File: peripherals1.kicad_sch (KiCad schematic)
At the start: 39 parts, among them Q1 Q_NMOS_GSD, SW3 SW_Push, SW4 SW_Push, SW5 SW_Push, SW6 SW_Push, U7 TSDP343xx

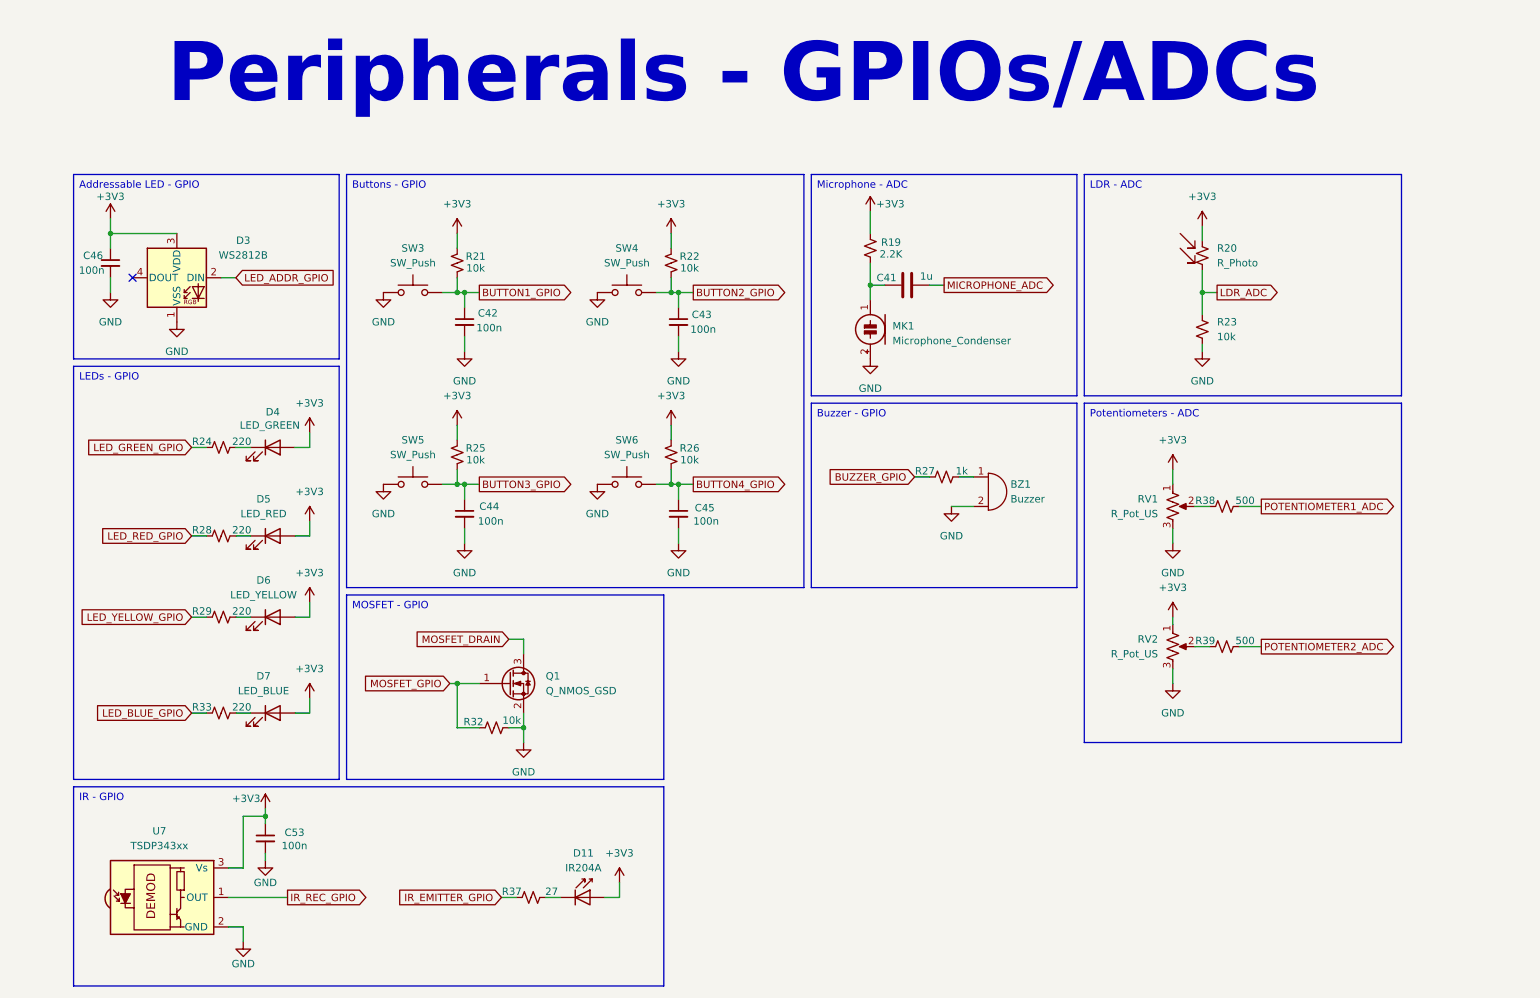
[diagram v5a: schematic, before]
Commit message: feat: adds footprints and new light sensor
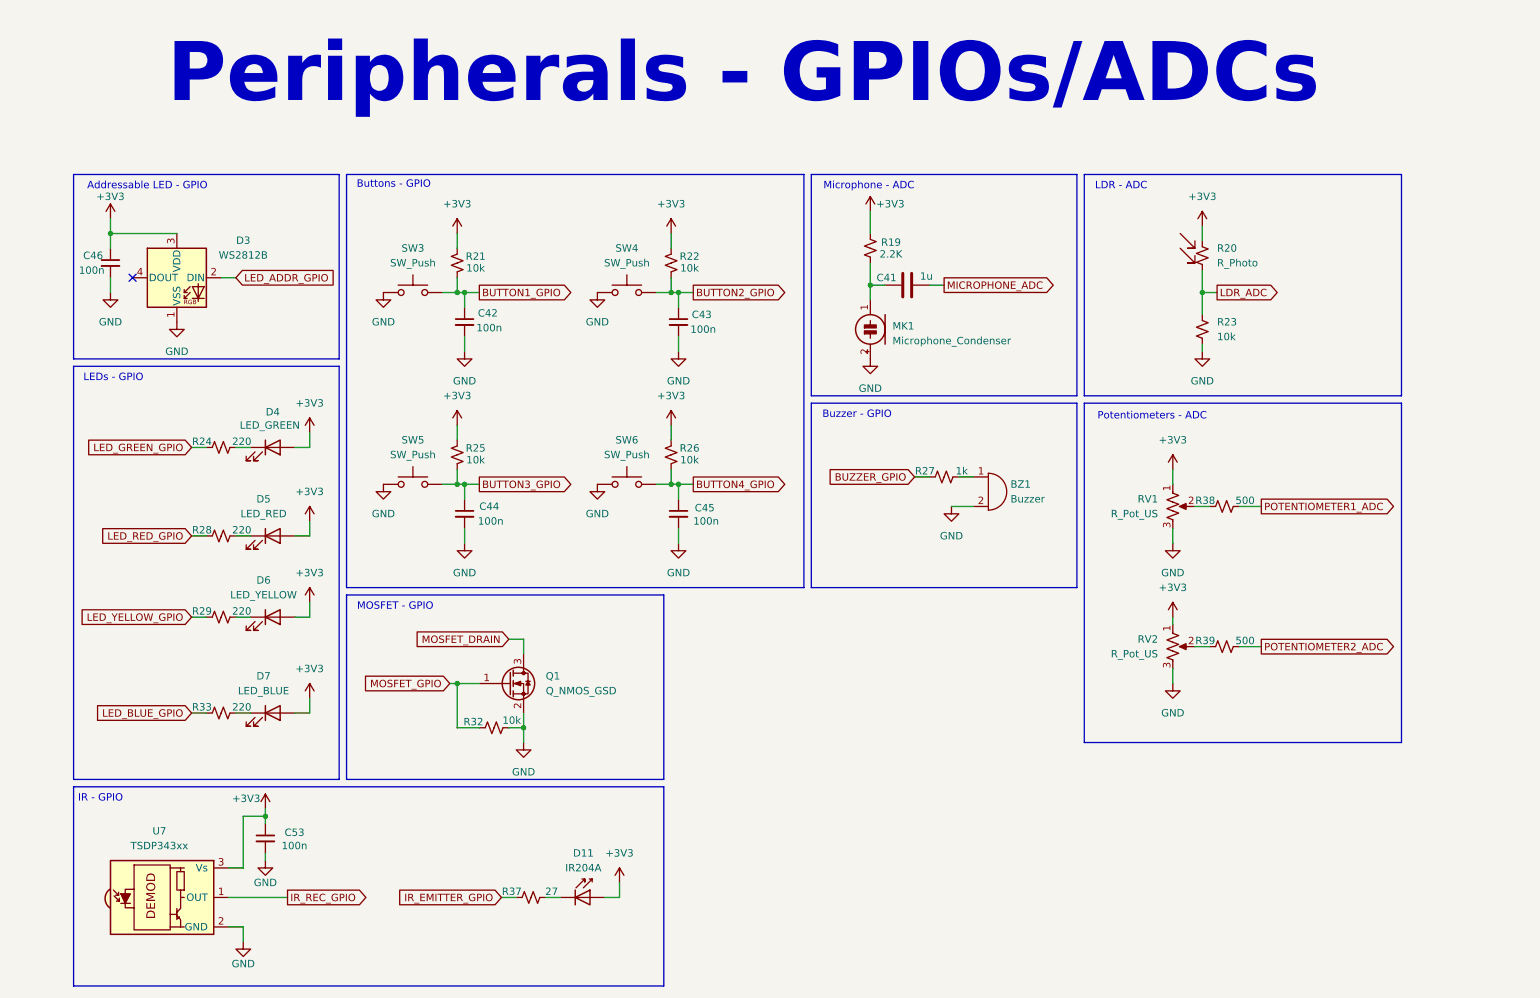
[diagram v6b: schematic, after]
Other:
- note added: "Addressable LED - GPIO"
- note added: "Buttons - GPIO"
- note added: "Buzzer - GPIO"
- note added: "IR - GPIO"
- note added: "LDR - ADC"
- note added: "LEDs - GPIO"
- note added: "MOSFET - GPIO"
- note added: "Microphone - ADC"
- note added: "Potentiometers - ADC"
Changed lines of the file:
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@@
 		(company "Os Circuitados")
+	)
+	(rectangle
+		(start 162.56 39.37)
+		(end 208.28 77.47)
+		(stroke
+			(width 0)
+			(type default)
+		)
+		(fill
+			(type none)
+		)
+	)
+	(rectangle
+		(start 209.55 39.37)
+		(end 264.16 77.47)
+		(stroke
+			(width 0)
+			(type default)
+		)
+		(fill
+			(type none)
+		)
+	)
+	(rectangle
+		(start 209.55 78.74)
+		(end 264.16 137.16)
+		(stroke
+			(width 0)
+			(type default)
+		)
+		(fill
+			(type none)
+		)
+	)
+	(rectangle
+		(start 82.55 111.76)
+		(end 137.16 143.51)
+		(stroke
+			(width 0)
+			(type default)
+		)
+		(fill
+			(type none)
+		)
+	)
+	(rectangle
+		(start 82.55 39.37)
+		(end 161.29 110.49)
+		(stroke
+			(width 0)
+			(type default)
+		)
+		(fill
+			(type none)
+		)
+	)
+	(rectangle
+		(start 35.56 39.37)
+		(end 81.28 71.12)
+		(stroke
+			(width 0)
+			(type default)
+		)
+		(fill
+			(type none)
+		)
+	)
+	(rectangle
+		(start 35.56 144.78)
+		(end 137.16 179.07)
+		(stroke
+			(width 0)
+			(type default)
+		)
+		(fill
+			(type none)
+		)
+	)
+	(rectangle
+		(start 162.56 78.74)
+		(end 208.28 110.49)
+		(stroke
+			(width 0)
+			(type default)
+		)
+		(fill
+			(type none)
+		)
+	)
+	(rectangle
+		(start 35.56 72.39)
+		(end 81.28 143.51)
+		(stroke
+			(width 0)
+			(type default)
+		)
+		(fill
+			(type none)
+		)
+	)
+	(text "Microphone - ADC"
+		(exclude_from_sim no)
+		(at 172.466 41.402 0)
+		(effects
+			(font
+				(size 1.27 1.27)
+			)
+		)
+	)
+	(text "Potentiometers - ADC"
+		(exclude_from_sim no)
+		(at 221.234 81.026 0)
+		(effects
+			(font
+				(size 1.27 1.27)
+			)
+		)
+	)
+	(text "LDR - ADC"
+		(exclude_from_sim no)
+		(at 215.9 41.402 0)
+		(effects
+			(font
+				(size 1.27 1.27)
+			)
+		)
+	)
+	(text "Buttons - GPIO"
+		(exclude_from_sim no)
+		(at 90.678 41.148 0)
+		(effects
+			(font
+				(size 1.27 1.27)
+			)
+		)
 	)
 	(text "Peripherals - GPIOs/ADCs"
@@
 		)
 	)
-	(text_box "Addressable LED - GPIO"
+	(text "MOSFET - GPIO"
 		(exclude_from_sim no)
-		(at 35.56 39.37 0)
-		(size 45.72 31.75)
-		(margins 0.9525 0.9525 0.9525 0.9525)
-		(stroke
-			(width 0)
-			(type solid)
-		)
-		(fill
-			(type none)
-		)
+		(at 90.932 113.792 0)
 		(effects
 			(font
 				(size 1.27 1.27)
 			)
-			(justify left top)
 		)
 	)
-	(text_box "IR - GPIO"
+	(text "Addressable LED - GPIO"
 		(exclude_from_sim no)
-		(at 35.56 144.78 0)
-		(size 101.6 34.29)
-		(margins 0.9525 0.9525 0.9525 0.9525)
-		(stroke
-			(width 0)
-			(type solid)
-		)
-		(fill
-			(type none)
-		)
+		(at 48.26 41.402 0)
 		(effects
 			(font
 				(size 1.27 1.27)
 			)
-			(justify left top)
 		)
 	)
-	(text_box "Microphone - ADC"
+	(text "IR - GPIO"
 		(exclude_from_sim no)
-		(at 162.56 39.37 0)
-		(size 45.72 38.1)
-		(margins 0.9525 0.9525 0.9525 0.9525)
-		(stroke
-			(width 0)
-			(type solid)
-		)
-		(fill
-			(type none)
-		)
+		(at 36.322 146.812 0)
 		(effects
 			(font
 				(size 1.27 1.27)
 			)
-			(justify left top)
+			(justify left)
 		)
 	)
-	(text_box "MOSFET - GPIO"
+	(text "LEDs - GPIO"
 		(exclude_from_sim no)
-		(at 82.55 111.76 0)
-		(size 54.61 31.75)
-		(margins 0.9525 0.9525 0.9525 0.9525)
-		(stroke
-			(width 0)
-			(type solid)
-		)
-		(fill
-			(type none)
-		)
+		(at 42.418 74.422 0)
 		(effects
 			(font
 				(size 1.27 1.27)
 			)
-			(justify left top)
 		)
 	)
-	(text_box "LDR - ADC"
+	(text "Buzzer - GPIO"
 		(exclude_from_sim no)
-		(at 209.55 39.37 0)
-		(size 54.61 38.1)
-		(margins 0.9525 0.9525 0.9525 0.9525)
-		(stroke
-			(width 0)
-			(type solid)
-		)
-		(fill
-			(type none)
-		)
+		(at 170.434 80.772 0)
 		(effects
 			(font
 				(size 1.27 1.27)
 			)
-			(justify left top)
 		)
 	)
-	(text_box "Buttons - GPIO"
-		(exclude_from_sim no)
-		(at 82.55 39.37 0)
-		(size 78.74 71.12)
-		(margins 0.9525 0.9525 0.9525 0.9525)
-		(stroke
-			(width 0)
-			(type solid)
-		)
-		(fill
-			(type none)
-		)
-		(effects
-			(font
-				(size 1.27 1.27)
-			)
-			(justify left top)
-		)
-	)
-	(text_box "Buzzer - GPIO"
-		(exclude_from_sim no)
-		(at 162.56 78.74 0)
-		(size 45.72 31.75)
-		(margins 0.9525 0.9525 0.9525 0.9525)
-		(stroke
-			(width 0)
-			(type solid)
-		)
-		(fill
-			(type none)
-		)
-		(effects
-			(font
-				(size 1.27 1.27)
-			)
-			(justify left top)
-		)
-	)
-	(text_box "Potentiometers - ADC"
-		(exclude_from_sim no)
-		(at 209.55 78.74 0)
-		(size 54.61 58.42)
-		(margins 0.9525 0.9525 0.9525 0.9525)
-		(stroke
-			(width 0)
-			(type solid)
-		)
-		(fill
-			(type none)
-		)
-		(effects
-			(font
-				(size 1.27 1.27)
-			)
-			(justify left top)
-		)
-	)
-	(text_box "LEDs - GPIO"
-		(exclude_from_sim no)
-		(at 35.56 72.39 0)
-		(size 45.72 71.12)
-		(margins 0.9525 0.9525 0.9525 0.9525)
-		(stroke
-			(width 0)
-			(type solid)
-		)
-		(fill
-			(type none)
-		)
-		(effects
-			(font
-				(size 1.27 1.27)
-			)
-			(justify left top)
-		)
-	)

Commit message: feat: connects all global labels
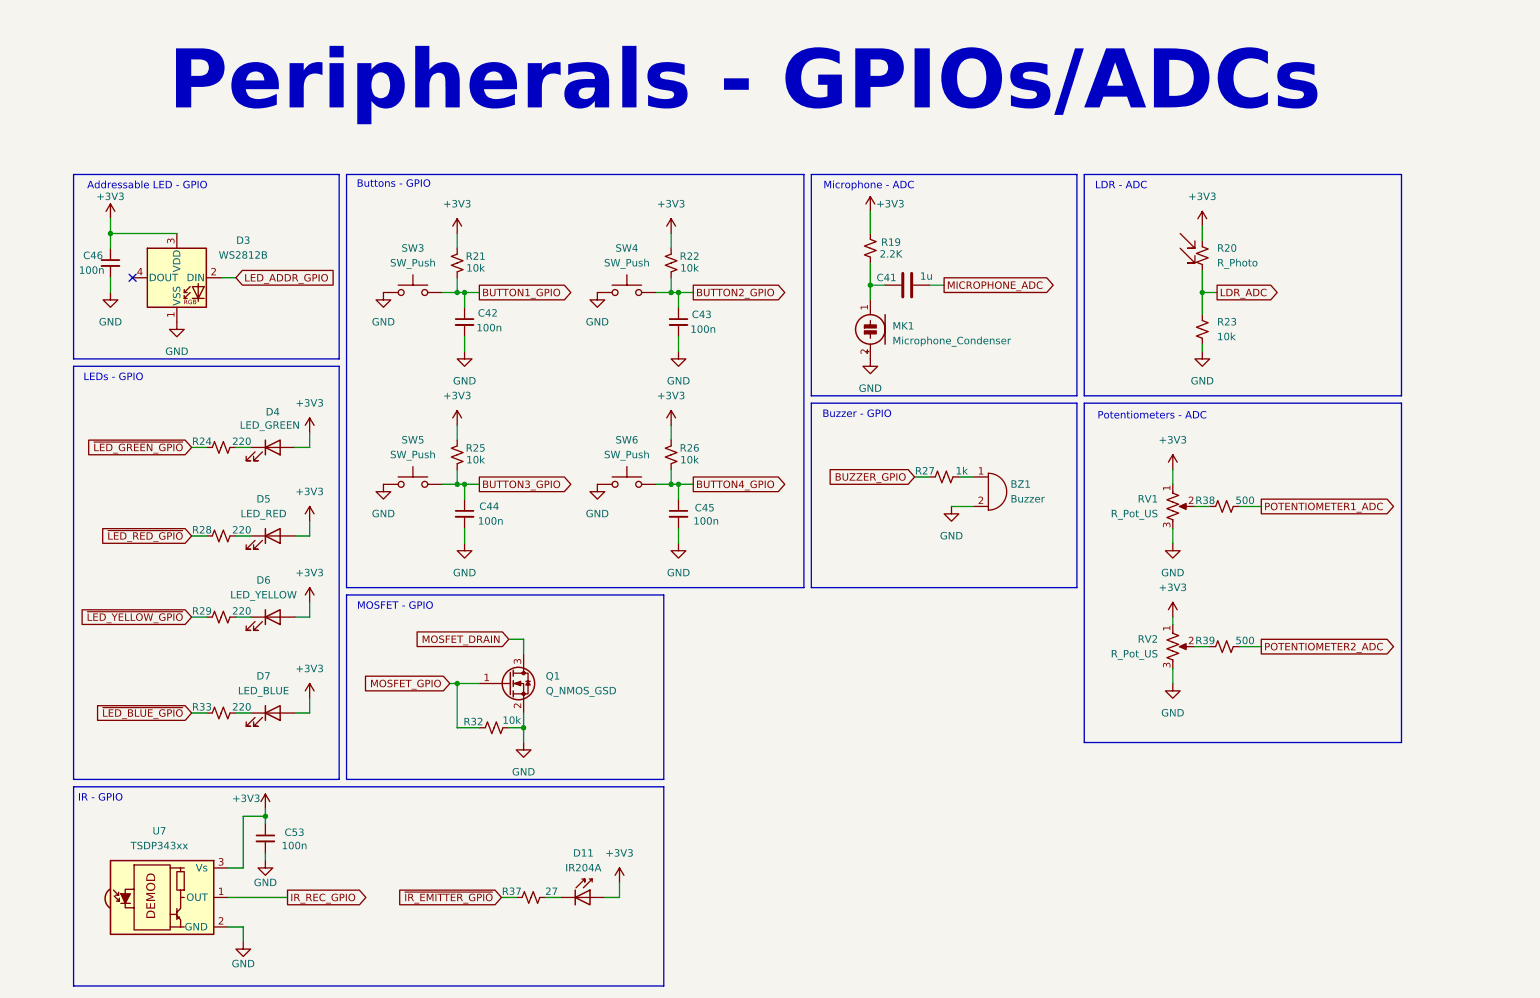
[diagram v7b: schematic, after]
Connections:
- net IR_EMITTER_GPIO renamed ~{IR_EMITTER_GPIO}
- net LED_BLUE_GPIO renamed ~{LED_BLUE_GPIO}
- net LED_GREEN_GPIO renamed ~{LED_GREEN_GPIO}
- net LED_RED_GPIO renamed ~{LED_RED_GPIO}
- net LED_YELLOW_GPIO renamed ~{LED_YELLOW_GPIO}
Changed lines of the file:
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@@
 	(text "Peripherals - GPIOs/ADCs"
 		(exclude_from_sim no)
-		(at 150.876 22.098 0)
+		(at 151.13 23.368 0)
 		(effects
 			(font
@@
 		)
 	)
-	(global_label "IR_EMITTER_GPIO"
+	(global_label "~{IR_EMITTER_GPIO}"
 		(shape input)
 		(at 109.22 163.83 180)
@@
 		)
 		(property "Intersheetrefs" "${INTERSHEET_REFS}"
-			(at 91.5014 163.83 0)
+			(at 90.3901 163.83 0)
 			(effects
 				(font
@@
 		)
 	)
-	(global_label "LED_BLUE_GPIO"
+	(global_label "~{LED_BLUE_GPIO}"
 		(shape input)
 		(at 55.88 132.08 180)
@@
 		)
 		(property "Intersheetrefs" "${INTERSHEET_REFS}"
-			(at 39.3709 132.08 0)
+			(at 38.2596 132.08 0)
 			(effects
 				(font
@@
 		)
 	)
-	(global_label "LED_RED_GPIO"
+	(global_label "~{LED_RED_GPIO}"
 		(shape input)
 		(at 55.88 101.6 180)
@@
 		)
 	)
-	(global_label "LED_YELLOW_GPIO"
+	(global_label "~{LED_YELLOW_GPIO}"
 		(shape input)
 		(at 55.88 115.57 180)
@@
 		)
 		(property "Intersheetrefs" "${INTERSHEET_REFS}"
-			(at 37.0728 115.57 0)
+			(at 35.9615 115.57 0)
 			(effects
 				(font
@@
 		)
 	)
-	(global_label "LED_GREEN_GPIO"
+	(global_label "~{LED_GREEN_GPIO}"
 		(shape input)
 		(at 55.88 86.36 180)

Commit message: chore: makes changes for DRC check compliance
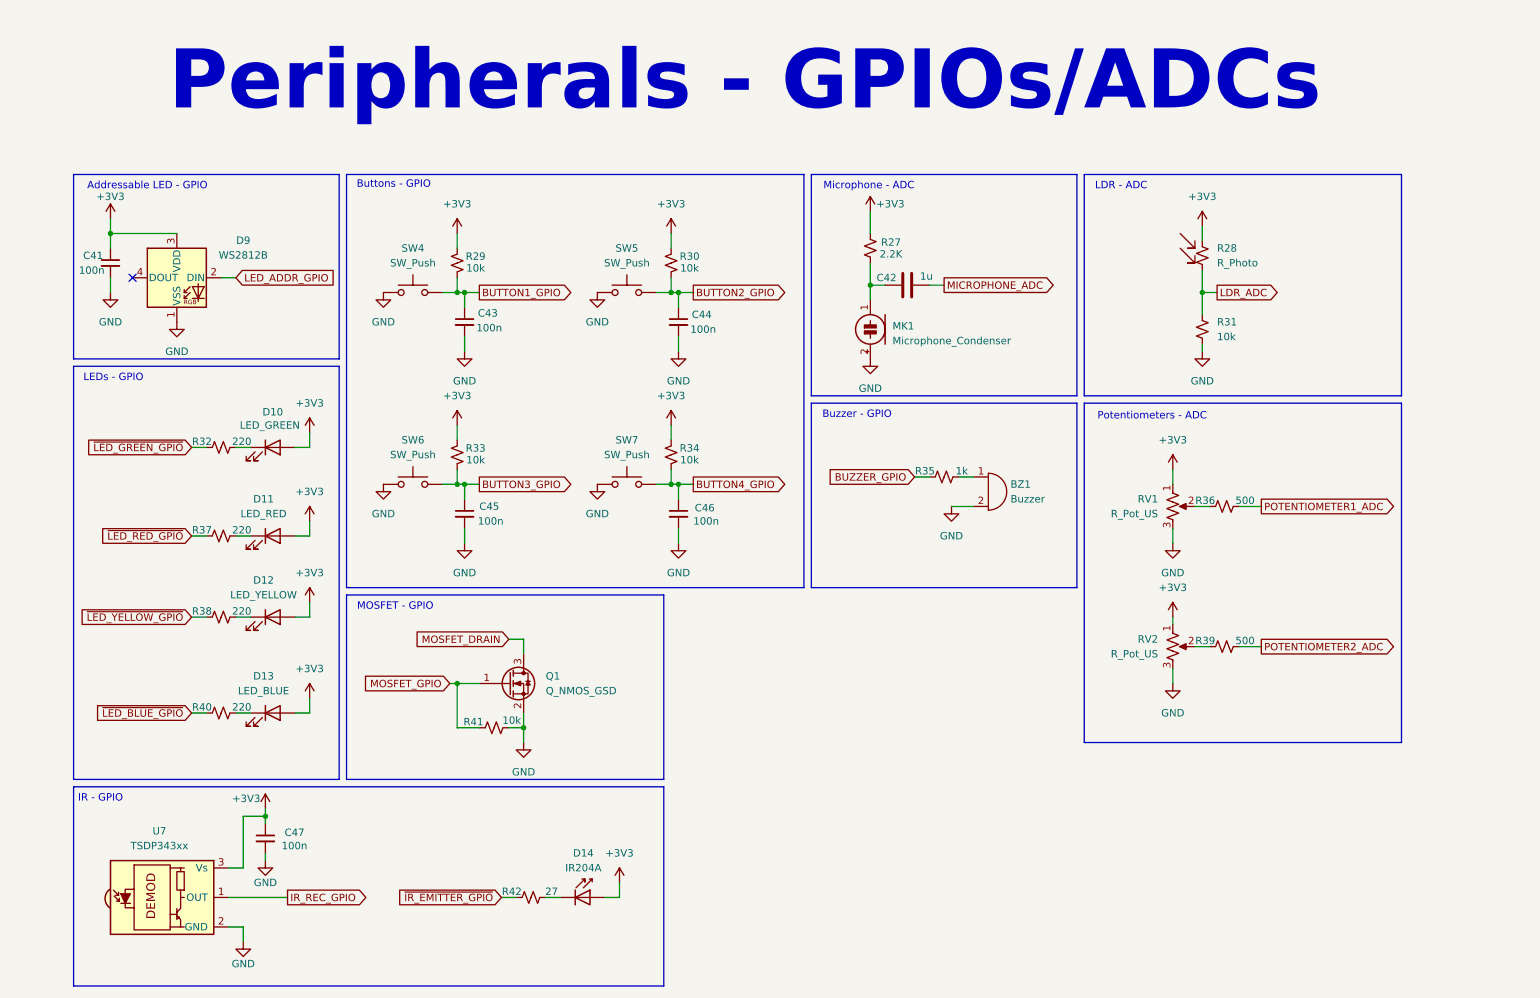
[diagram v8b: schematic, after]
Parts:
- renumbered C46 to C41, C41 to C42, C42 to C43, C43 to C44, C44 to C45, C45 to C46, C53 to C47, D4 to D10, D5 to D11, D6 to D12, D7 to D13, D11 to D14, D3 to D9, R19 to R27, R20 to R28, R21 to R29, R22 to R30, R23 to R31, R24 to R32, R25 to R33, R26 to R34, R27 to R35, R38 to R36, R28 to R37, R29 to R38, R33 to R40, R32 to R41, R37 to R42, SW3 to SW4, SW4 to SW5, SW5 to SW6, SW6 to SW7
